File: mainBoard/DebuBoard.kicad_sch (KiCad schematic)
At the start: 9 parts, among them J1 Conn_01x04, J31 Conn_02x05_Odd_Even, J7 Conn_01x05

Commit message: ukild
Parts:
- added J10: Conn_02x07_Odd_Even, Connector_PinHeader_1.27mm:PinHeader_2x07_P1.27mm_Vertical_SMD, symbol Connector_Generic:Conn_02x07_Odd_Even
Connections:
- net GND: now also J31.3 (Pin_3), J31.5 (Pin_5), J10.11 (Pin_11), J10.5 (Pin_5), J10.7 (Pin_7)
- net DB-TUNING-LINES.SWDIO: now reaches J31.2 (Pin_2)
- net DB-TUNING-LINES.SWDIO: now also J10.4 (Pin_4)
- net DB-TUNING-LINES.SWCLK: now reaches J31.4 (Pin_4)
- net DB-TUNING-LINES.SWCLK: now also J10.6 (Pin_6)
- new net DB-TUNING-LINES.NRST: J10.12 (Pin_12)
- new net DB-TUNING-LINES.RX-2: J10.13 (Pin_13)
- new net DB-TUNING-LINES.TX-2: J10.14 (Pin_14)
- no-connect marks 3 -> 6
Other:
- moved on the sheet: J31

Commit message: DebugBoard
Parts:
- added J33: Conn_01x04, Connector_PinHeader_2.54mm:PinHeader_1x04_P2.54mm_Vertical, symbol Connector_Generic:Conn_01x04
- added J34, J35, J37, J38: Conn_01x02, Connector_PinHeader_2.54mm:PinHeader_1x02_P2.54mm_Vertical, symbol Connector_Generic:Conn_01x02
- J31: footprint (none) -> Connector_PinHeader_1.27mm:PinHeader_2x05_P1.27mm_Vertical
- J32: renamed from J10; footprint Connector_PinHeader_1.27mm:PinHeader_2x07_P1.27mm_Vertical_SMD -> Connector_PinHeader_1.27mm:PinHeader_2x07_P1.27mm_Vertical
- renumbered J7 to J23, J1 to J24, J7 to J25, J7 to J26, J7 to J27, J1 to J28, J1 to J29, J1 to J30
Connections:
- net DB-TUNING-LINES.NRST: now also J31.10 (Pin_10)
- net DB-TUNING-LINES.RX-2: now also J31.7 (Pin_7)
- net DB-TUNING-LINES.TX-2: now also J31.9 (Pin_9)
- net GND: now also J33.4 (Pin_4), J34.1 (Pin_1), J34.2 (Pin_2), J35.1 (Pin_1), J35.2 (Pin_2), J37.1 (Pin_1), J37.2 (Pin_2), J38.1 (Pin_1), J38.2 (Pin_2)
- net DB-TUNING-LINES.TRACESWO: now reaches J31.6 (Pin_6)
- new net DB-DRV.CURRENT: J33.3 (Pin_3)
- new net DB-DRV.IN1: J33.1 (Pin_1)
- new net DB-DRV.IN2: J33.2 (Pin_2)
- no-connect marks 6 -> 7
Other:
- moved on the sheet: J30

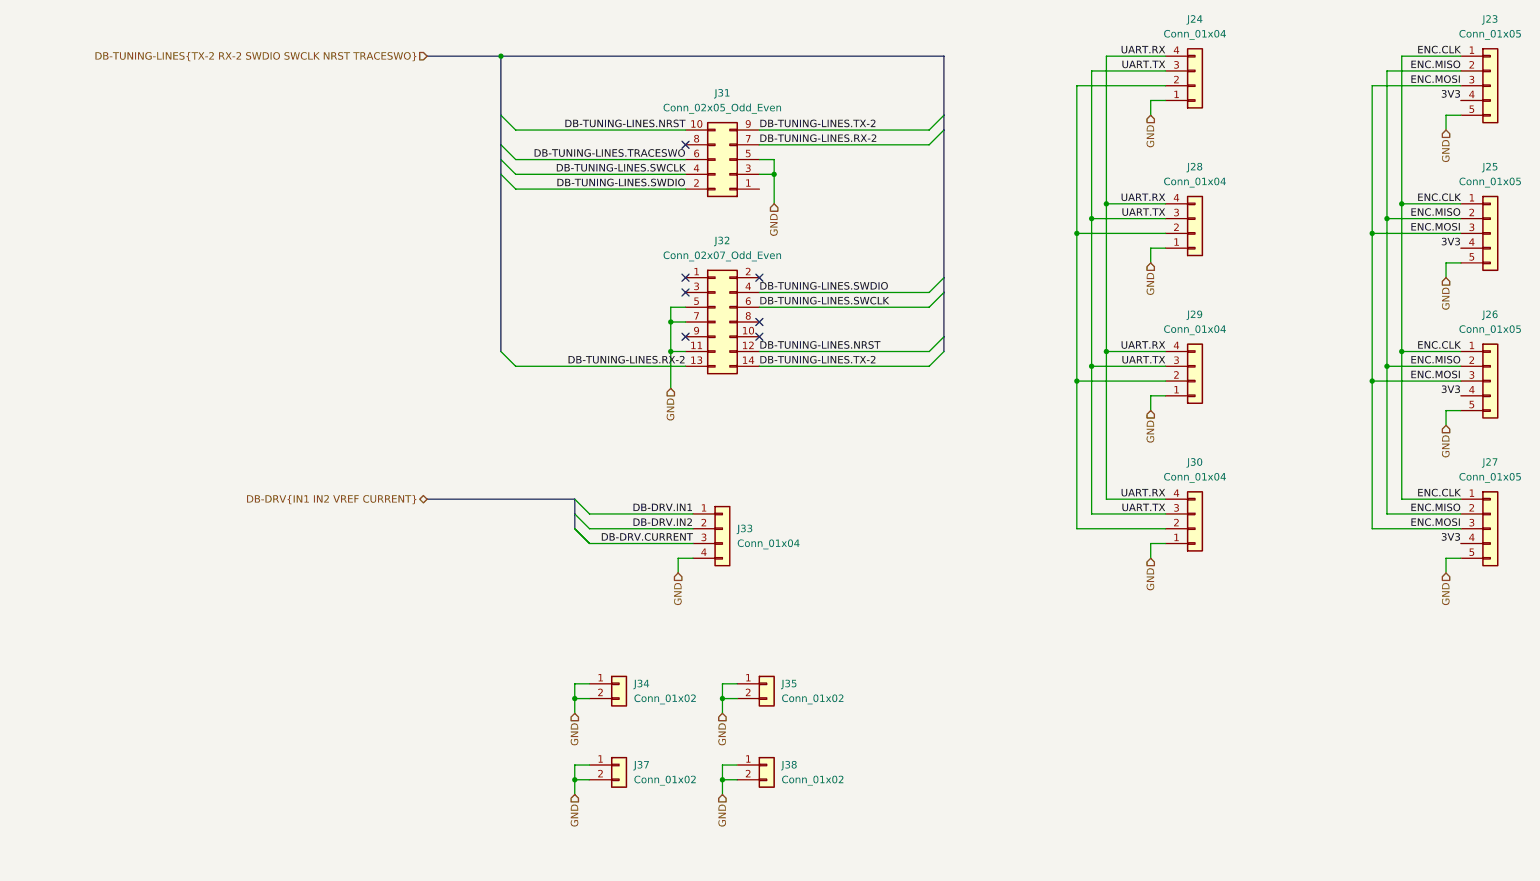
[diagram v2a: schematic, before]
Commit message: Add power LEDs and UART connector
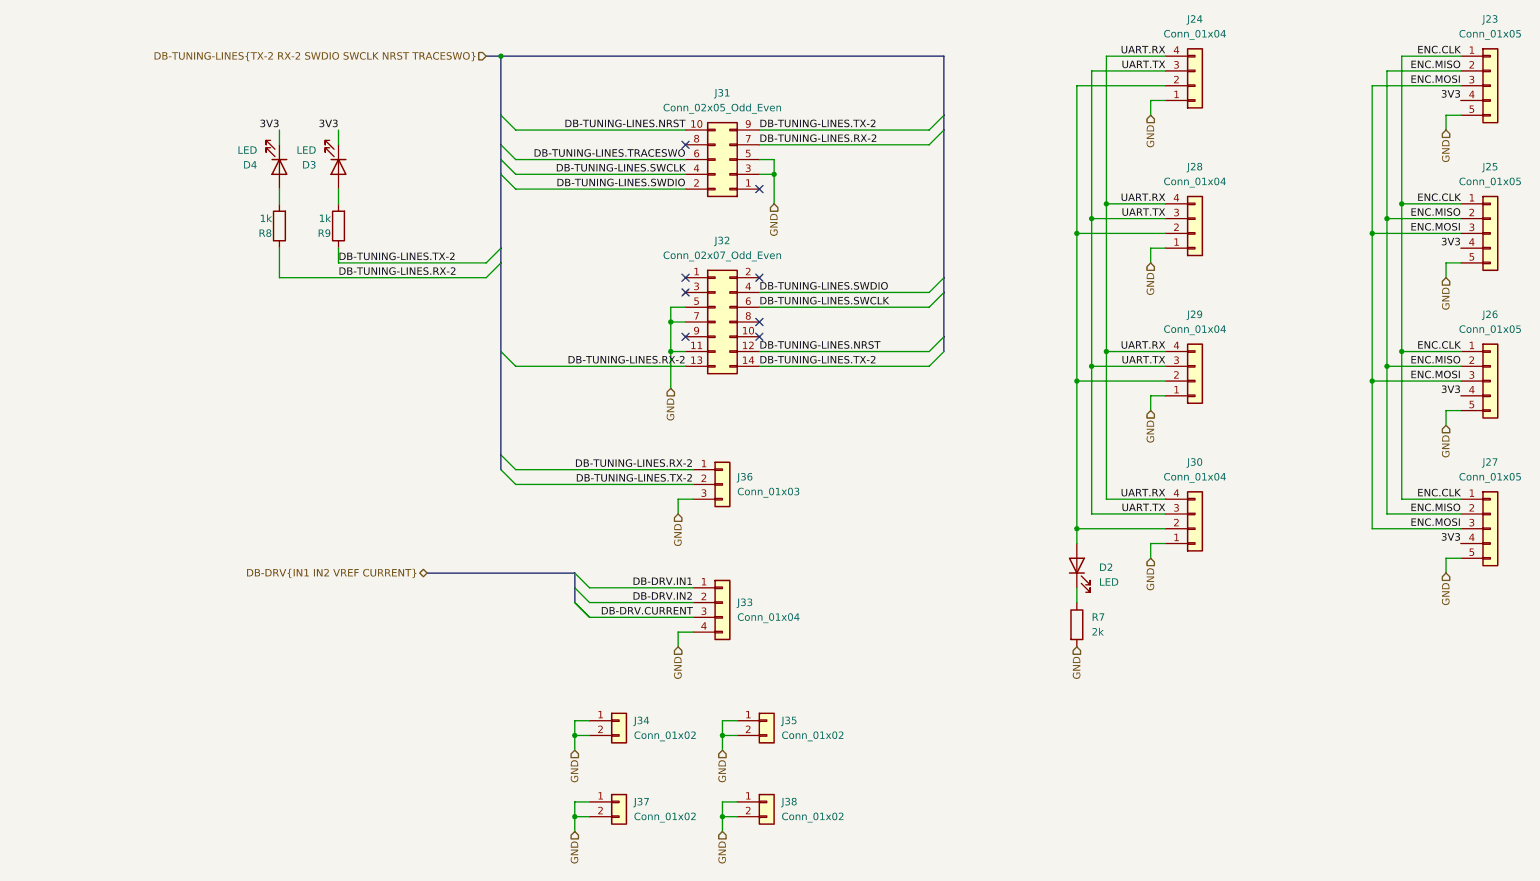
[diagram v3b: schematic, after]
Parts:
- added D2, D3, D4: LED, LED_SMD:LED_0603_1608Metric, symbol Device:LED
- added J36: Conn_01x03, Connector_PinHeader_2.54mm:PinHeader_1x03_P2.54mm_Vertical, symbol Connector_Generic:Conn_01x03
- added R7: 2k, Capacitor_SMD:C_0603_1608Metric, symbol Device:R
- added R8, R9: 1k, Capacitor_SMD:C_0603_1608Metric, symbol Device:R
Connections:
- net 3V3: now also D3.1 (K), D4.1 (K)
- net DB-TUNING-LINES.RX-2: now also J36.1 (Pin_1), R8.1
- net DB-TUNING-LINES.TX-2: now also J36.2 (Pin_2), R9.1
- net GND: now also J36.3 (Pin_3), R7.2
- net at J24.2 (Pin_2), J28.2 (Pin_2), J29.2 (Pin_2)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: now also D2.2 (A)
- new net: D4.2 (A), R8.2
- new net: D2.1 (K), R7.1
- new net: D3.2 (A), R9.2
- no-connect marks 7 -> 8
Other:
- moved on the sheet: J33, J34, J35, J37, J38

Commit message: Add LCSC code
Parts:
- D2, D3, D4: LCSC (none) -> C7496820
- J23, J25, J26, J27: LCSC (none) -> C7501286
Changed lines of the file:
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@@
+      (effects (font (size 1.27 1.27)) hide)
+    )
+    (property "LCSC" "C7501286" (at 259.08 68.58 0)
       (effects (font (size 1.27 1.27)) hide)
     )
@@
       (effects (font (size 1.27 1.27)) hide)
     )
+    (property "LCSC" "C7496820" (at 187.96 125.73 0)
+      (effects (font (size 1.27 1.27)) hide)
+    )
     (pin "2")
     (pin "1")
@@
       (effects (font (size 1.27 1.27)) hide)
     )
+    (property "LCSC" "C7496820" (at 50.8 57.15 0)
+      (effects (font (size 1.27 1.27)) hide)
+    )
     (pin "2")
     (pin "1")
@@
       (effects (font (size 1.27 1.27)) hide)
     )
+    (property "LCSC" "C7501286" (at 259.08 93.98 0)
+      (effects (font (size 1.27 1.27)) hide)
+    )
     (pin "1")
     (pin "2")
@@
       (effects (font (size 1.27 1.27)) hide)
     )
+    (property "LCSC" "C7496820" (at 60.96 57.15 0)
+      (effects (font (size 1.27 1.27)) hide)
+    )
     (pin "2")
     (pin "1")
@@
       (effects (font (size 1.27 1.27)) hide)
     )
+    (property "LCSC" "C7501286" (at 259.08 43.18 0)
+      (effects (font (size 1.27 1.27)) hide)
+    )
     (pin "1")
     (pin "2")
@@
       (effects (font (size 1.27 1.27)) hide)
     )
+    (property "LCSC" "C7501286" (at 259.08 119.38 0)
+      (effects (font (size 1.27 1.27)) hide)
+    )

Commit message: LCSC cods
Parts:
- J24, J28, J29, J30: LCSC (none) -> C20598724
- J31: LCSC (none) -> C239059
- J33: LCSC (none) -> C2691448
- J34, J35, J37, J38: LCSC (none) -> C492401
- J36: LCSC (none) -> C49257
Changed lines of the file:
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@@
+      (effects (font (size 1.27 1.27)) hide)
+    )
+    (property "LCSC" "C492401" (at 134.62 166.37 0)
       (effects (font (size 1.27 1.27)) hide)
     )
@@
       (effects (font (size 1.27 1.27)) hide)
     )
+    (property "LCSC" "C20598724" (at 208.28 93.98 0)
+      (effects (font (size 1.27 1.27)) hide)
+    )
     (pin "1")
     (pin "2")
@@
     )
     (property "Datasheet" "~" (at 128.27 55.88 0)
+      (effects (font (size 1.27 1.27)) hide)
+    )
+    (property "LCSC" "C239059" (at 128.27 55.88 0)
       (effects (font (size 1.27 1.27)) hide)
     )
@@
       (effects (font (size 1.27 1.27)) hide)
     )
+    (property "LCSC" "C2691448" (at 127 132.08 0)
+      (effects (font (size 1.27 1.27)) hide)
+    )
     (pin "3")
     (pin "4")
@@
       (effects (font (size 1.27 1.27)) hide)
     )
+    (property "LCSC" "C492401" (at 109.22 166.37 0)
+      (effects (font (size 1.27 1.27)) hide)
+    )
     (pin "1")
     (pin "2")
@@
     )
     (property "note" "" (at 208.28 68.58 0)
+      (effects (font (size 1.27 1.27)) hide)
+    )
+    (property "LCSC" "C20598724" (at 208.28 68.58 0)
       (effects (font (size 1.27 1.27)) hide)
     )
@@
       (effects (font (size 1.27 1.27)) hide)
     )
+    (property "LCSC" "C492401" (at 109.22 152.4 0)
+      (effects (font (size 1.27 1.27)) hide)
+    )
     (pin "1")
     (pin "2")
@@
     )
     (property "note" "" (at 208.28 119.38 0)
+      (effects (font (size 1.27 1.27)) hide)
+    )
+    (property "LCSC" "C20598724" (at 208.28 119.38 0)
       (effects (font (size 1.27 1.27)) hide)
     )
@@
       (effects (font (size 1.27 1.27)) hide)
     )
+    (property "LCSC" "C49257" (at 127 111.76 0)
+      (effects (font (size 1.27 1.27)) hide)
+    )
     (pin "3")
     (pin "1")
@@
       (effects (font (size 1.27 1.27)) hide)
     )
+    (property "LCSC" "C20598724" (at 208.28 43.18 0)
+      (effects (font (size 1.27 1.27)) hide)
+    )
     (pin "1")
     (pin "2")
@@
       (effects (font (size 1.27 1.27)) hide)
     )
+    (property "LCSC" "C492401" (at 134.62 152.4 0)
+      (effects (font (size 1.27 1.27)) hide)
+    )

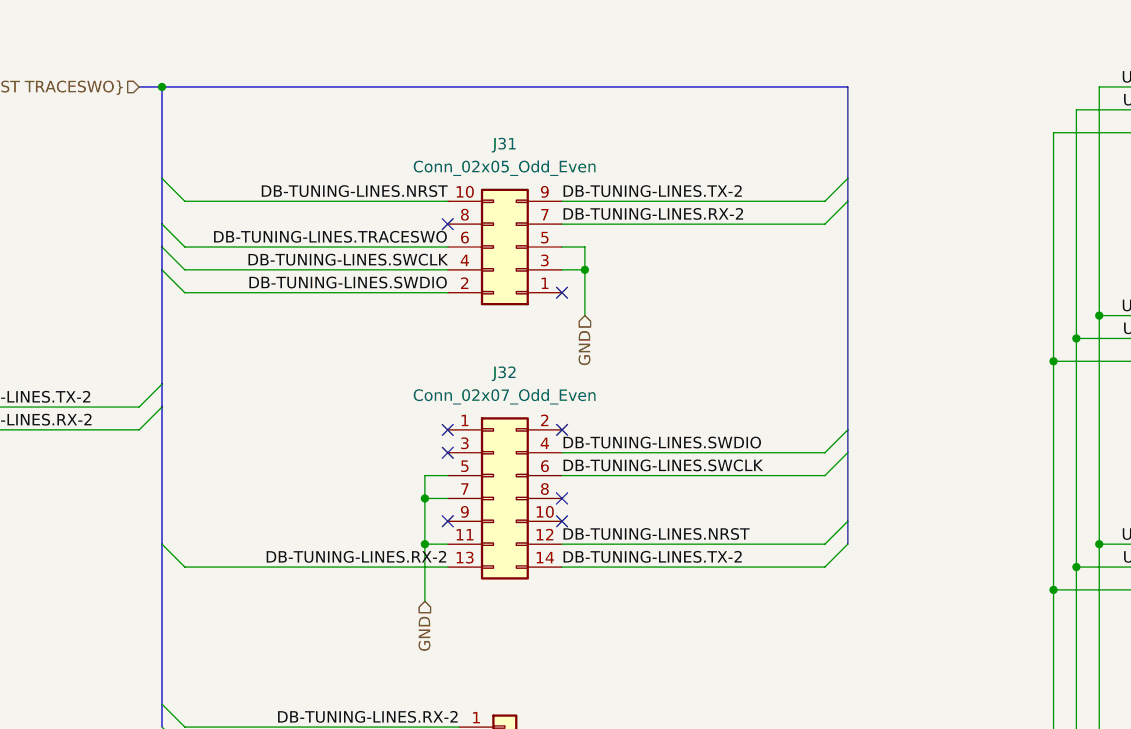
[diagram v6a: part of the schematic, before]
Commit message: On debug board, For BMDU connector (J31) - make TX/RX wiring optional
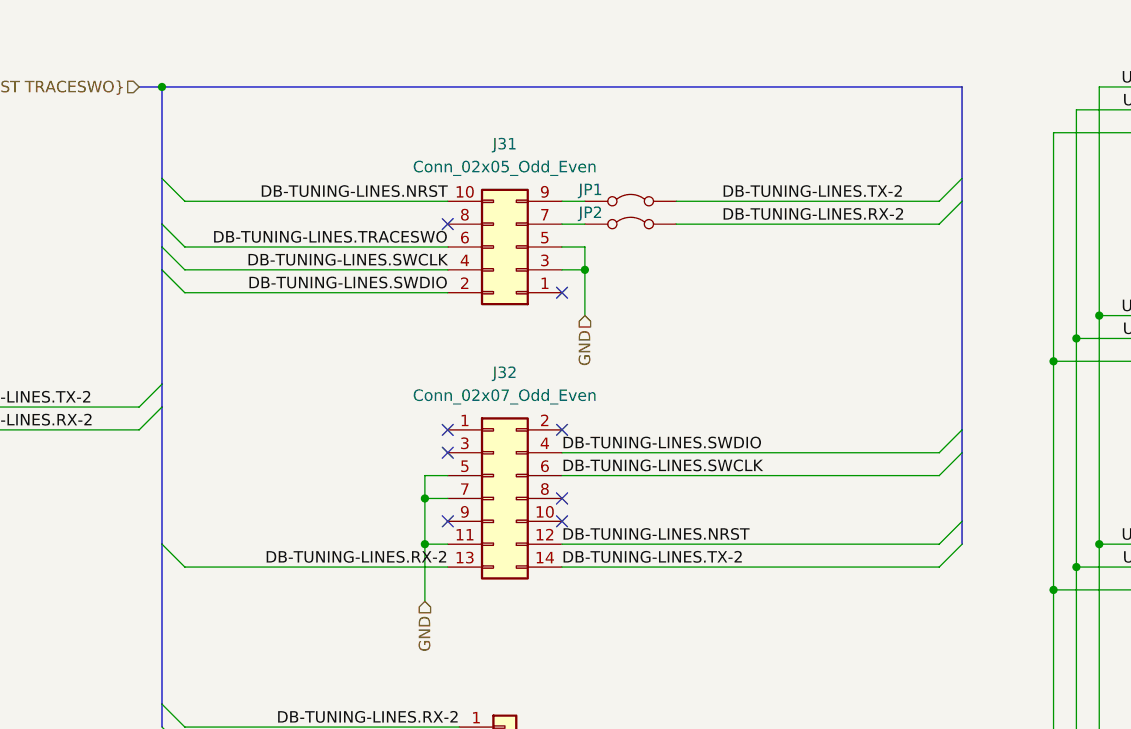
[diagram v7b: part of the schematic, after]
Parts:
- added JP1, JP2: Jumper_2_Bridged, Jumper:SolderJumper-2_P1.3mm_Open_TrianglePad1.0x1.5mm, symbol Jumper:Jumper_2_Bridged
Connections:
- net DB-TUNING-LINES.RX-2: now also JP2.2 (B); no longer J31.7 (Pin_7)
- net DB-TUNING-LINES.TX-2: now also JP1.2 (B); no longer J31.9 (Pin_9)
- new net: J31.9 (Pin_9), JP1.1 (A)
- new net: J31.7 (Pin_7), JP2.1 (A)
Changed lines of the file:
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@@
 	)
 	(bus_entry
-		(at 165.1 50.8)
+		(at 177.8 50.8)
 		(size -2.54 2.54)
 		(stroke
@@
 	)
 	(bus_entry
-		(at 165.1 48.26)
+		(at 177.8 48.26)
 		(size -2.54 2.54)
 		(stroke
@@
 	)
 	(bus_entry
-		(at 165.1 86.36)
+		(at 177.8 86.36)
 		(size -2.54 2.54)
 		(stroke
@@
 	)
 	(bus_entry
-		(at 165.1 88.9)
+		(at 177.8 88.9)
 		(size -2.54 2.54)
 		(stroke
@@
 	)
 	(bus_entry
-		(at 165.1 76.2)
+		(at 177.8 76.2)
 		(size -2.54 2.54)
 		(stroke
@@
 	)
 	(bus_entry
-		(at 165.1 78.74)
+		(at 177.8 78.74)
 		(size -2.54 2.54)
 		(stroke
@@
 	(bus
 		(pts
-			(xy 165.1 78.74) (xy 165.1 86.36)
+			(xy 177.8 78.74) (xy 177.8 86.36)
+		)
+		(stroke
+			(width 0)
+			(type default)
+		)
+	)
+	(wire
+		(pts
+			(xy 146.05 53.34) (xy 175.26 53.34)
 		)
 		(stroke
@@
 	(bus
 		(pts
-			(xy 165.1 38.1) (xy 165.1 48.26)
-		)
-		(stroke
-			(width 0)
-			(type default)
-		)
-	)
-	(wire
-		(pts
-			(xy 133.35 50.8) (xy 162.56 50.8)
+			(xy 177.8 38.1) (xy 177.8 48.26)
+		)
+		(stroke
+			(width 0)
+			(type default)
+		)
+	)
+	(wire
+		(pts
+			(xy 133.35 50.8) (xy 135.89 50.8)
 		)
 		(stroke
@@
 	(bus
 		(pts
-			(xy 165.1 48.26) (xy 165.1 50.8)
+			(xy 177.8 48.26) (xy 177.8 50.8)
 		)
 		(stroke
@@
 	(bus
 		(pts
-			(xy 165.1 76.2) (xy 165.1 78.74)
+			(xy 177.8 76.2) (xy 177.8 78.74)
 		)
 		(stroke
@@
 	(wire
 		(pts
+			(xy 146.05 50.8) (xy 175.26 50.8)
+		)
+		(stroke
+			(width 0)
+			(type default)
+		)
+	)
+	(wire
+		(pts
 			(xy 118.11 83.82) (xy 118.11 88.9)
 		)
@@
 	(wire
 		(pts
-			(xy 133.35 78.74) (xy 162.56 78.74)
+			(xy 133.35 78.74) (xy 175.26 78.74)
 		)
 		(stroke
@@
 	(bus
 		(pts
-			(xy 165.1 86.36) (xy 165.1 88.9)
+			(xy 88.9 38.1) (xy 177.8 38.1)
+		)
+		(stroke
+			(width 0)
+			(type default)
+		)
+	)
+	(bus
+		(pts
+			(xy 177.8 86.36) (xy 177.8 88.9)
 		)
 		(stroke
@@
 	(wire
 		(pts
-			(xy 133.35 81.28) (xy 162.56 81.28)
+			(xy 133.35 81.28) (xy 175.26 81.28)
 		)
 		(stroke
@@
 	(wire
 		(pts
-			(xy 133.35 53.34) (xy 162.56 53.34)
+			(xy 133.35 53.34) (xy 135.89 53.34)
 		)
 		(stroke
@@
 	(bus
 		(pts
-			(xy 165.1 50.8) (xy 165.1 76.2)
+			(xy 177.8 50.8) (xy 177.8 76.2)
 		)
 		(stroke
@@
 	(wire
 		(pts
-			(xy 133.35 88.9) (xy 162.56 88.9)
+			(xy 133.35 88.9) (xy 175.26 88.9)
 		)
 		(stroke
@@
 	(wire
 		(pts
-			(xy 133.35 91.44) (xy 162.56 91.44)
+			(xy 133.35 91.44) (xy 175.26 91.44)
 		)
 		(stroke
@@
 		)
 	)
-	(bus
-		(pts
-			(xy 88.9 38.1) (xy 165.1 38.1)
-		)
-		(stroke
-			(width 0)
-			(type default)
-		)
-	)
 	(wire
 		(pts
@@
 	)
 	(label "DB-TUNING-LINES.RX-2"
-		(at 133.35 53.34 0)
+		(at 151.13 53.34 0)
 		(fields_autoplaced yes)
 		(effects
@@
 	)
 	(label "DB-TUNING-LINES.TX-2"
-		(at 133.35 50.8 0)
+		(at 151.13 50.8 0)
 		(fields_autoplaced yes)
 		(effects
@@
 			)
 			(justify right)
+		)
+	)
+	(symbol
+		(lib_id "Jumper:Jumper_2_Bridged")
+		(at 140.97 50.8 0)
+		(unit 1)
+		(exclude_from_sim yes)
+		(in_bom yes)
+		(on_board yes)
+		(dnp no)
+		(property "Reference" "JP1"
+			(at 136.525 49.53 0)
+			(effects
+				(font
+					(size 1.27 1.27)
+				)
+			)
+		)
+		(property "Value" "Jumper_2_Bridged"
+			(at 140.97 48.26 0)
+			(effects
+				(font
+					(size 1.27 1.27)
+				)
+				(hide yes)
+			)
+		)
+		(property "Footprint" "Jumper:SolderJumper-2_P1.3mm_Open_TrianglePad1.0x1.5mm"
+			(at 140.97 50.8 0)
+			(effects
+				(font
+					(size 1.27 1.27)
+				)
+				(hide yes)
+			)
+		)
+		(property "Datasheet" "~"
+			(at 140.97 50.8 0)
+			(effects
+				(font
+					(size 1.27 1.27)
+				)
+				(hide yes)
+			)
+		)
+		(property "Description" "Jumper, 2-pole, closed/bridged"
+			(at 140.97 50.8 0)
+			(effects
+				(font
+					(size 1.27 1.27)
+				)
+				(hide yes)
+			)
+		)
+		(pin "1"
+		)
+		(pin "2"
+		)
+		(instances
+			(project ""
+				(path "/30ed06d7-0b03-4878-b461-066cda7e7438/3f547cb3-b336-4e37-a735-70b4a8f64673"
+					(reference "JP1")
+					(unit 1)
+				)
+			)
 		)
 	)
@@
 					(unit 1)
 				)
+			)
+		)
+	)
+	(symbol
+		(lib_id "Jumper:Jumper_2_Bridged")
+		(at 140.97 53.34 0)
+		(unit 1)
+		(exclude_from_sim yes)
+		(in_bom yes)
+		(on_board yes)
+		(dnp no)
+		(property "Reference" "JP2"
+			(at 136.525 52.07 0)
+			(effects
+				(font
+					(size 1.27 1.27)
+				)
+			)
+		)
+		(property "Value" "Jumper_2_Bridged"
+			(at 140.97 50.8 0)
+			(effects
+				(font
+					(size 1.27 1.27)
+				)
+				(hide yes)
+			)
+		)
+		(property "Footprint" "Jumper:SolderJumper-2_P1.3mm_Open_TrianglePad1.0x1.5mm"
+			(at 140.97 53.34 0)
+			(effects
+				(font
+					(size 1.27 1.27)
+				)
+				(hide yes)
+			)
+		)
+		(property "Datasheet" "~"
+			(at 140.97 53.34 0)
+			(effects
+				(font
+					(size 1.27 1.27)
+				)
+				(hide yes)
+			)
+		)
+		(property "Description" "Jumper, 2-pole, closed/bridged"
+			(at 140.97 53.34 0)
+			(effects
+				(font
+					(size 1.27 1.27)
+				)
+				(hide yes)
+			)
+		)
+		(pin "1"
+		)
+		(pin "2"
+		)
+		(instances
+			(project "mainBoard"
+				(path "/30ed06d7-0b03-4878-b461-066cda7e7438/3f547cb3-b336-4e37-a735-70b4a8f64673"
+					(reference "JP2")
+					(unit 1)
+				)
